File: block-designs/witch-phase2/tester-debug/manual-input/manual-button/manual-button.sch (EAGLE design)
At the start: 8 parts

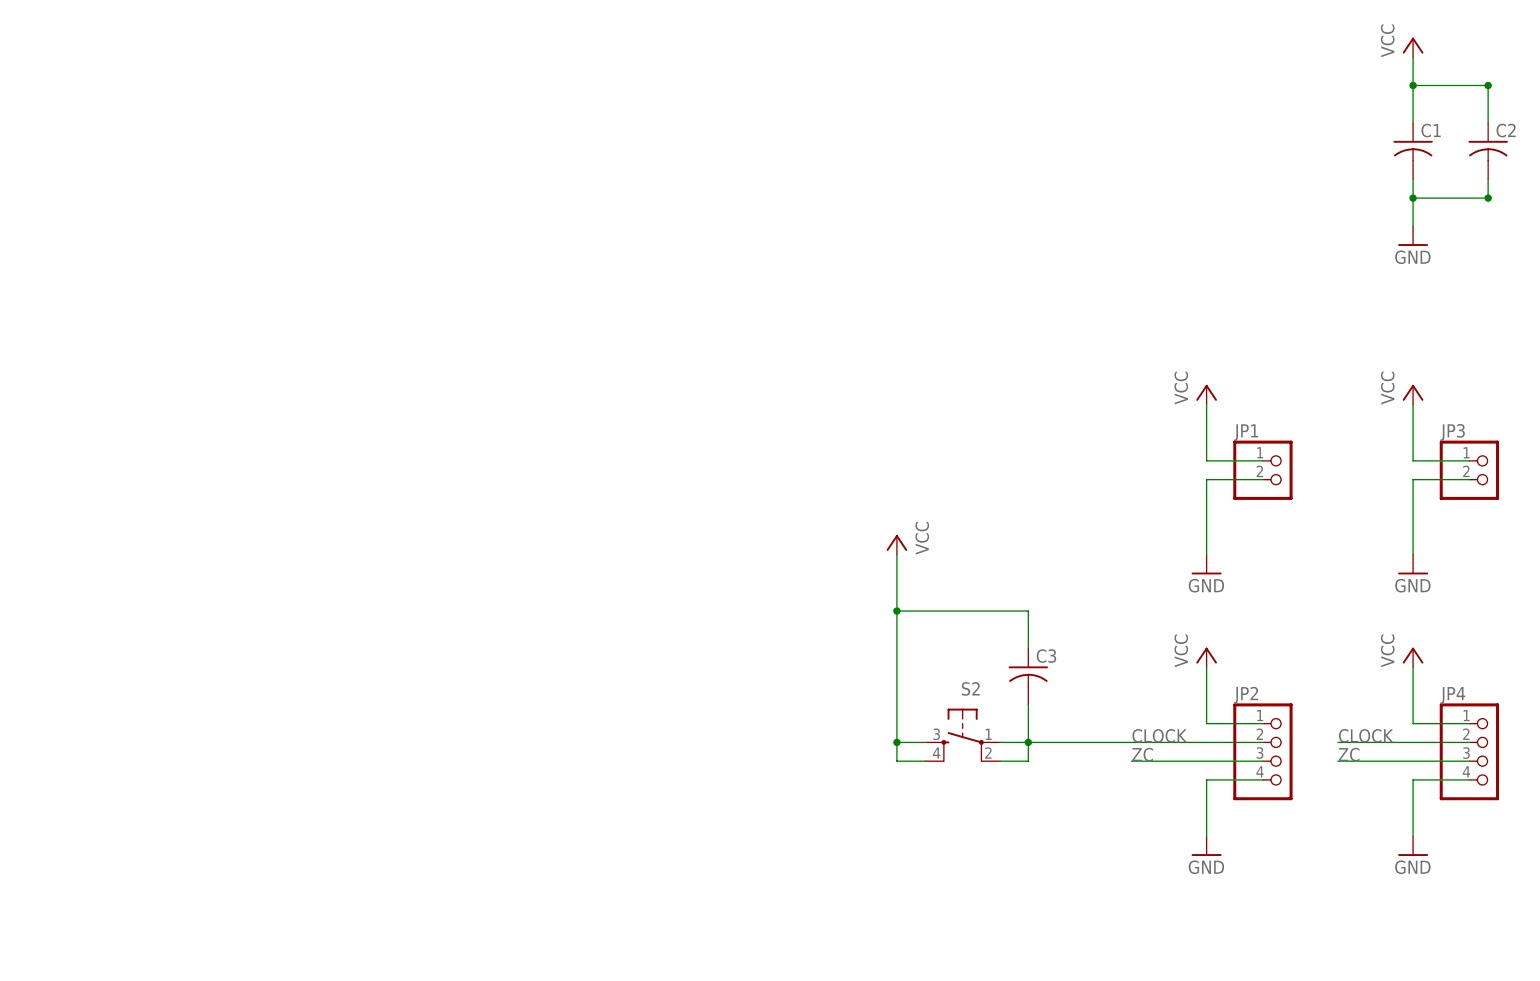
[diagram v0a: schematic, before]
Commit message: switch to using a schmitt trigger with OR gate for clock output
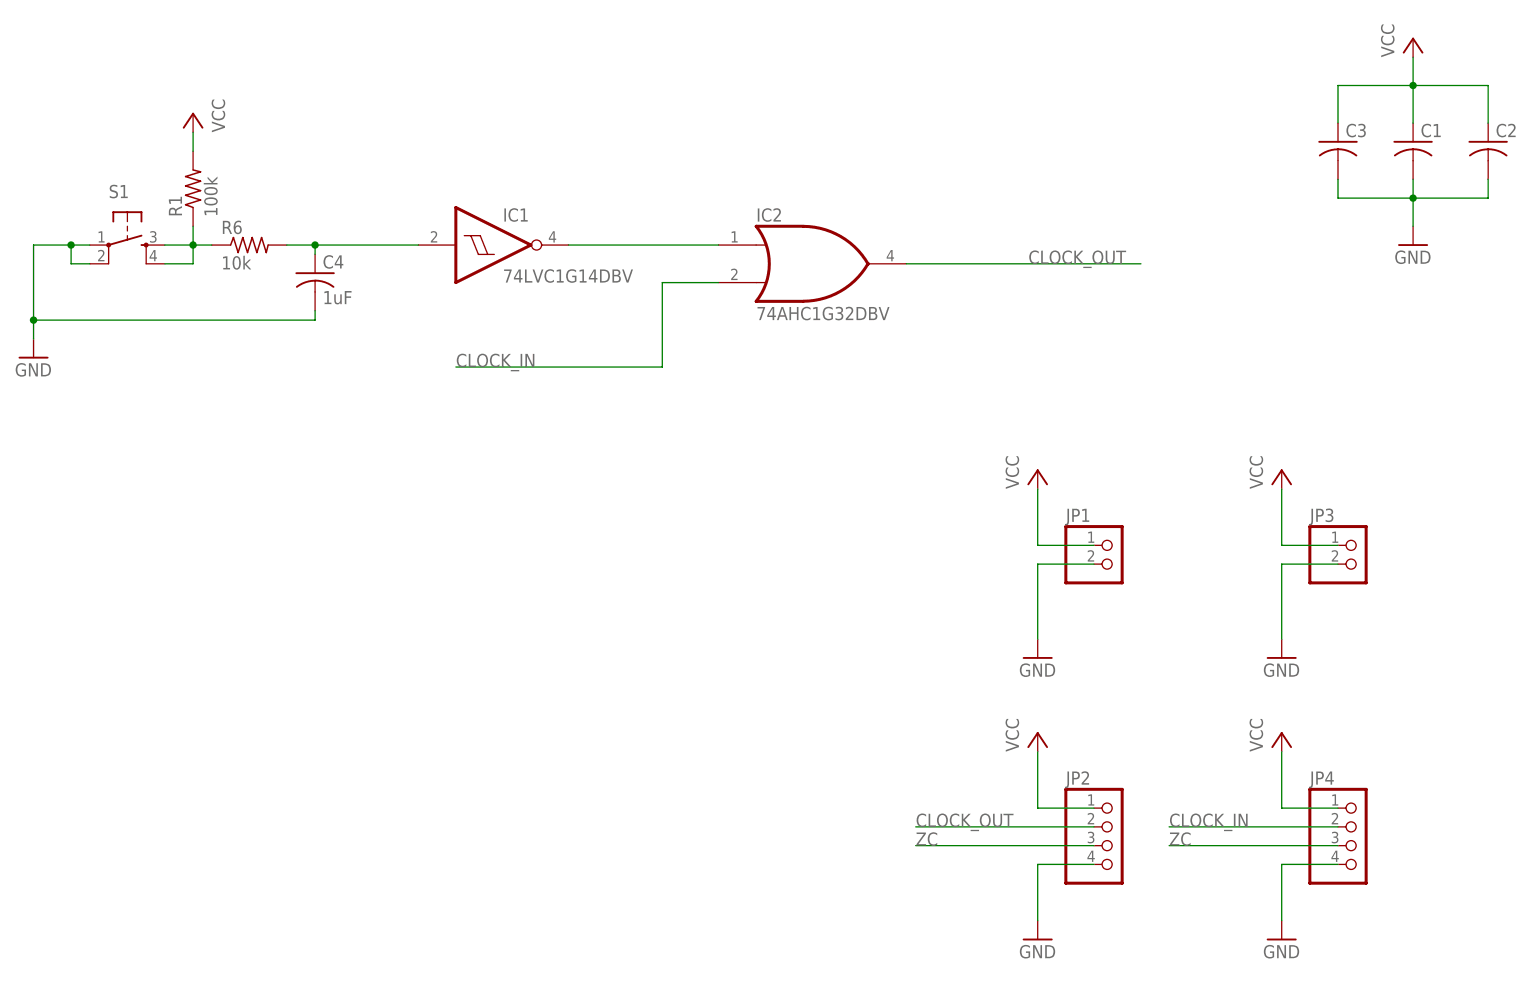
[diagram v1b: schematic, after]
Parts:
- removed S2: (no value), SparkFun-Electromechanical:TAC_SWITCHPTH
- added C4: 1uF, resistor:C-USC0603K
- added IC1: 74LVC1G14DBV, 74xx-little-us:74LVC1G14DBV
- added IC2: 74AHC1G32DBV, 74xx-little-us:74AHC1G32DBV
- added R1: 100k, resistor:R-US_R0603
- added R6: 10k, resistor:R-US_R0603
- added S1: (no value), SparkFun-Electromechanical:TAC_SWITCHPTH
- C1, C2, C3: device resistor:C-USC0805 -> resistor:C-USC0603K
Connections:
- removed net CLOCK: C3.2, JP2.2, JP4.2, S2.1, S2.2
- new net CLOCK_IN: IC2A.I1, JP4.2
- new net CLOCK_OUT: IC2A.O, JP2.2
- new net DA_IN: IC1A.O, IC2A.I0
- new net N$1: R1.1, R6.1, S1.3, S1.4
- new net N$2: C4.1, IC1A.I, R6.2
- net GND: now also C3.2, C4.2, S1.1, S1.2
- net VCC: now also R1.2; no longer S2.3, S2.4
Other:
- moved on the sheet: C3, JP1, JP2, JP3, JP4
